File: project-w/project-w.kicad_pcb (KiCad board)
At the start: 2 copper layers, 17 parts, among them U1 NE555, U2 CD4017

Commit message: adding trace routes
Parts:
- removed BT1: Battery_Cell, Connectors_USB:USB_Micro-B_Wuerth-629105150521
- added J1: USB_A, Connectors_USB:USB_Micro-B_Molex-105017-0001, F.Cu at (184.2, 96.5)
- moved U2 50.9 mm to (180.3, 104.1)
- moved R3 48.7 mm to (176.5, 94.0), turned to 270 degrees
- moved C1 40.6 mm to (168.9, 96.5)
- moved U1 39.0 mm to (167.6, 114.3)
- moved R2 38.3 mm to (167.6, 109.2)
- moved R1 38.2 mm to (167.6, 104.1)
- moved D4 29.8 mm to (158.8, 111.8)
- moved D3 29.4 mm to (158.8, 104.1)
- moved D5 27.0 mm to (153.7, 118.1)
- moved D2 25.7 mm to (153.7, 97.8)
- moved D6 22.0 mm to (146.1, 120.7)
- moved D1 20.7 mm to (146.1, 94.0)
- moved D7 14.9 mm to (138.4, 118.1)
- moved D10 12.4 mm to (138.4, 97.8)
- moved D8 6.73 mm to (133.3, 111.8)
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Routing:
- net Net-(D1-Pad1): track 0.00 -> 100.8 mm
- net Net-(D2-Pad2): track 0.00 -> 67.4 mm, vias 0 -> 2
- net Net-(C1-Pad2): track 0.00 -> 64.7 mm, vias 0 -> 1
- net Net-(D10-Pad2): track 0.00 -> 64.0 mm, vias 0 -> 1
- net Net-(J1-Pad1): track 0.00 -> 56.6 mm, vias 0 -> 1
- net Net-(D5-Pad2): track 0.00 -> 50.5 mm, vias 0 -> 1
- net Net-(U1-Pad3): track 0.00 -> 50.5 mm
- net Net-(D1-Pad2): track 0.00 -> 50.1 mm
- net Net-(D8-Pad2): track 0.00 -> 47.6 mm
- net Net-(D9-Pad2): track 0.00 -> 46.6 mm
- net Net-(D7-Pad2): track 0.00 -> 45.2 mm, vias 0 -> 1
- net Net-(D6-Pad2): track 0.00 -> 39.9 mm
- net Net-(D3-Pad2): track 0.00 -> 38.8 mm
- net Net-(C1-Pad1): track 0.00 -> 35.2 mm
- net Net-(D4-Pad2): track 0.00 -> 28.8 mm
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
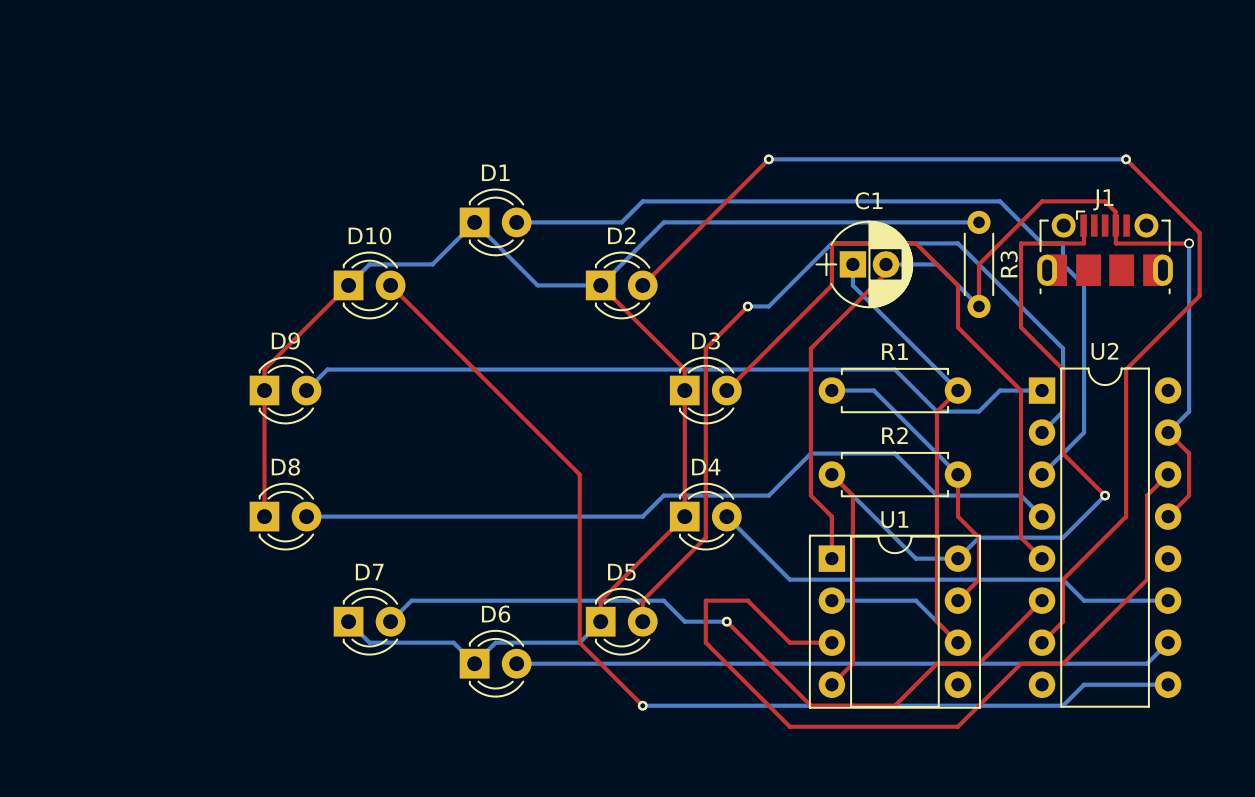
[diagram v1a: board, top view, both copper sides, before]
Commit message: adding more space for silk screening
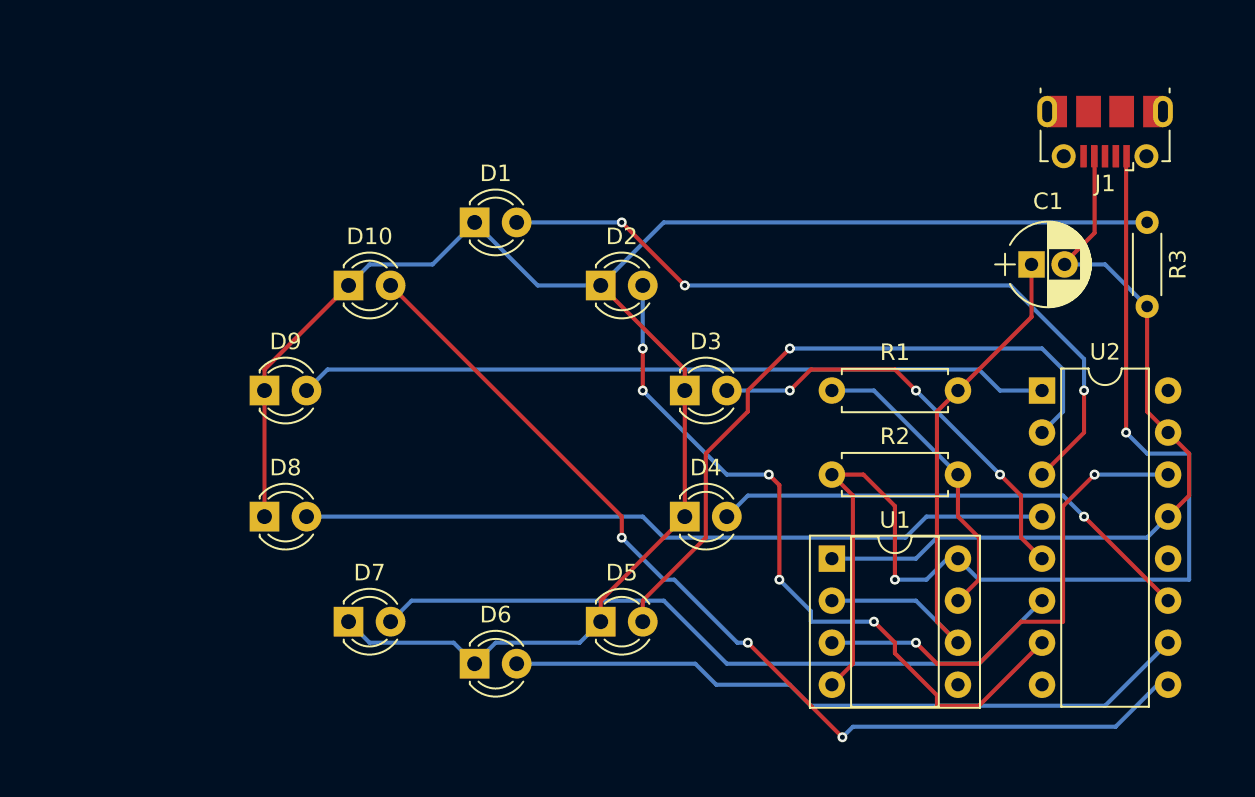
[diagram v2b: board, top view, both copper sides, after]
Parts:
- moved C1 10.8 mm to (179.7, 96.5)
- moved R3 10.2 mm to (186.7, 94.0)
- moved J1 8.89 mm to (184.2, 87.6), turned to 180 degrees
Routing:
- net Net-(D2-Pad2): track 67.4 -> 44.4 mm, vias 2 -> 5
- net Net-(U1-Pad3): track 50.5 -> 29.7 mm, vias 0 -> 2
- net Net-(C1-Pad2): track 64.7 -> 49.1 mm, vias 1 -> 0
- net Net-(J1-Pad1): track 56.6 -> 70.3 mm, vias 1 -> 2
- net Net-(D3-Pad2): track 38.8 -> 25.8 mm, vias 0 -> 3
- net Net-(D1-Pad1): track 100.8 -> 110.9 mm
- net Net-(D5-Pad2): track 50.5 -> 41.6 mm
- net Net-(D1-Pad2): track 50.1 -> 45.7 mm, vias 0 -> 3
- net Net-(D10-Pad2): track 64.0 -> 60.4 mm, vias 1 -> 3
- net Net-(D8-Pad2): track 47.6 -> 45.5 mm
- net Net-(D7-Pad2): track 45.2 -> 43.1 mm, vias 1 -> 0
- net Net-(D6-Pad2): track 39.9 -> 42.0 mm
- net Net-(D4-Pad2): track 28.8 -> 29.8 mm, vias 0 -> 1
- net Net-(D9-Pad2): track 46.6 -> 45.5 mm
- net Net-(C1-Pad1): track 35.2 -> 34.4 mm

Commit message: adding example text
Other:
- board text added: "Lorem Ipsum #0004"
- board text added: "blah blah __________________________ foo bar baz etc. etc. etc. etc."
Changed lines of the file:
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@@
     (area 131.974999 83.205 189.625 125.895002)
     (thickness 1.6)
-    (drawings 0)
+    (drawings 2)
     (tracks 170)
     (zones 0)
@@
     )
   )
+  (gr_text "blah blah __________________________\nfoo bar baz\netc. etc. etc. etc." (at 177.8 88.9) (layer B.SilkS)
+    (effects (font (size 1.5 1.5) (thickness 0.3)) (justify left mirror))
+  )
+  (gr_text "Lorem Ipsum #0004" (at 154.94 86.36) (layer F.SilkS)
+    (effects (font (size 2 2) (thickness 0.4)))
+  )
   (segment (start 175.26 104.14) (end 179.705 99.695) (width 0.25) (layer F.Cu) (net 1) (status 80000))

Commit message: trying to fix 3d models
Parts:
- J1: footprint Connectors_USB:USB_Micro-B_Molex-105017-0001 -> Connectors_USB:USB_Micro-B_Molex_47346-0001
- U1: footprint Housings_DIP:DIP-8_W7.62mm_Socket -> Housings_DIP:DIP-8_W7.62mm

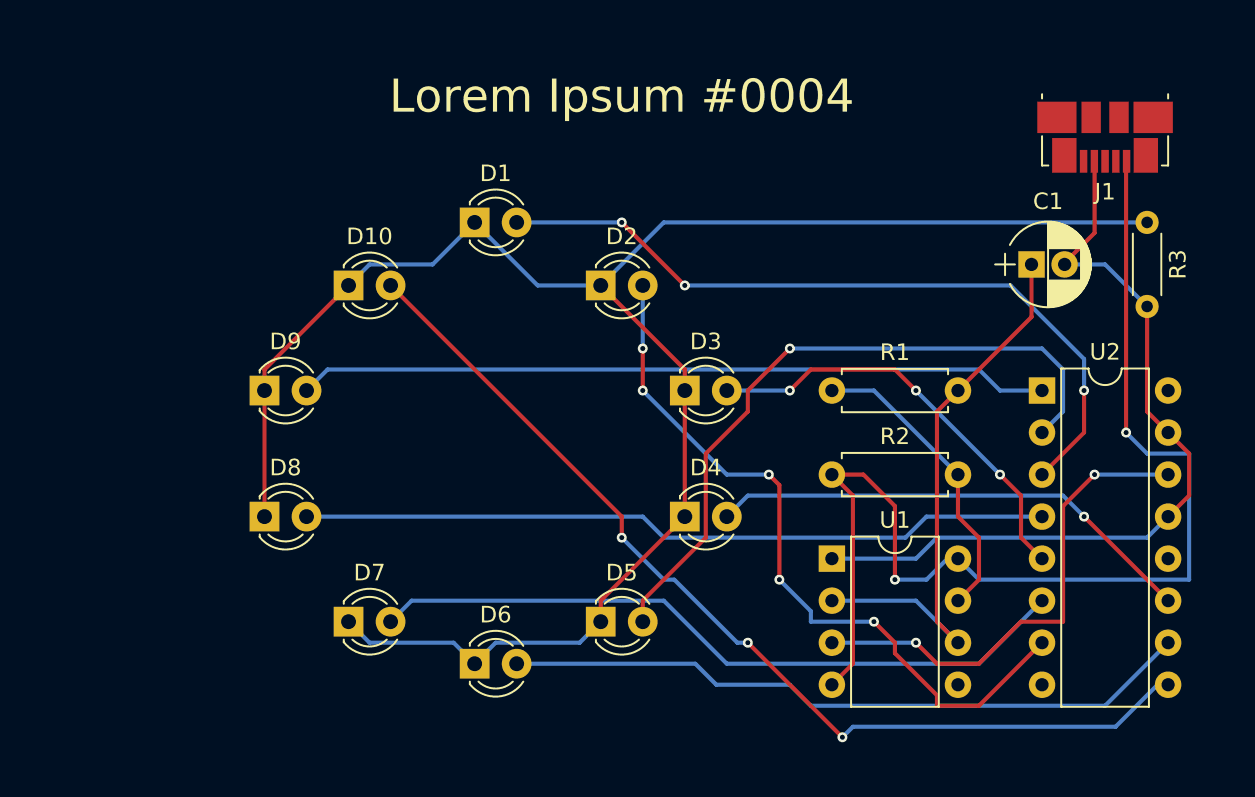
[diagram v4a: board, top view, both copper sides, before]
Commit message: updating schematic to fix VSS VDD issues
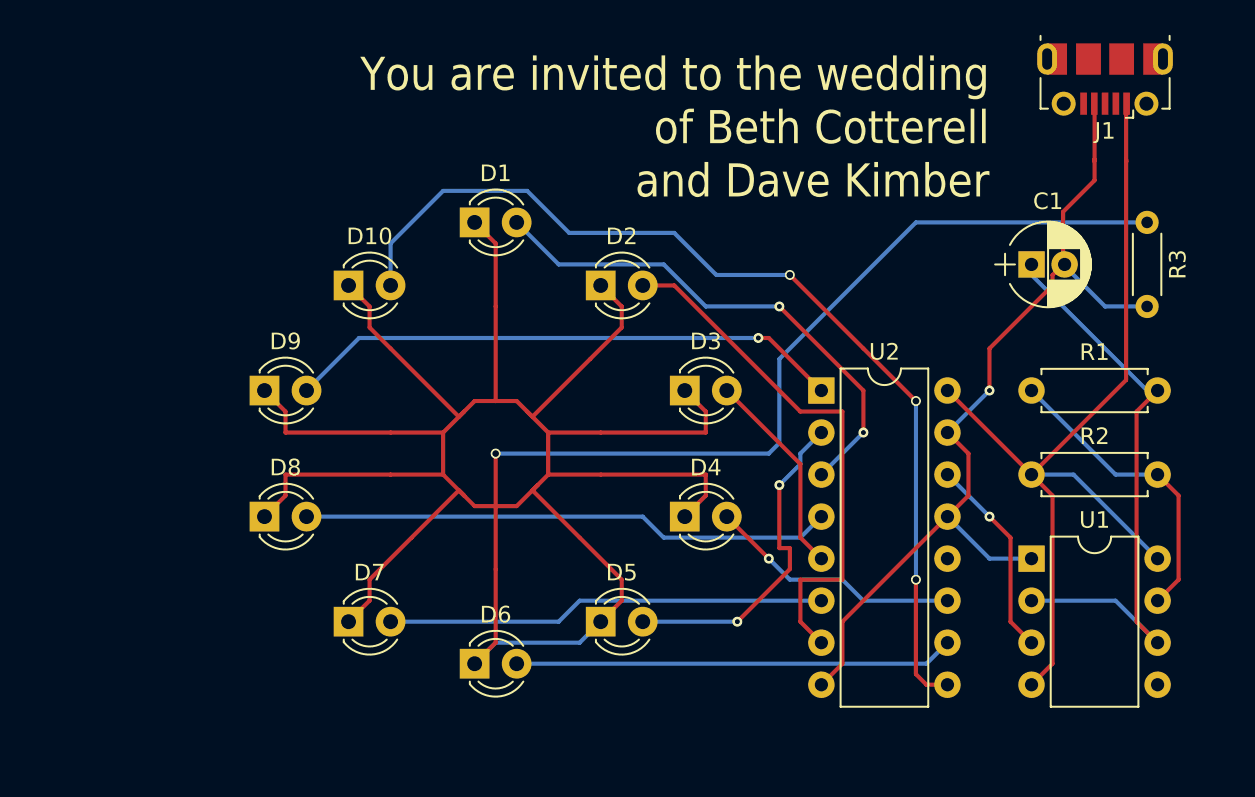
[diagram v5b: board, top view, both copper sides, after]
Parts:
- J1: footprint Connectors_USB:USB_Micro-B_Molex_47346-0001 -> Connectors_USB:USB_Micro-B_Molex-105017-0001
- R1: value 1K -> 47K
- moved U2 13.3 mm to (167.0, 104.1)
- moved R1 12.1 mm to (179.7, 104.1)
- moved R2 12.1 mm to (179.7, 109.2)
- moved U1 12.1 mm to (179.7, 114.3)
- moved J1 3.17 mm to (184.2, 84.5)
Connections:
- C1 pad 2: Net-(C1-Pad2) -> VSS
- J1 pad 1: Net-(J1-Pad1) -> VDD
- J1 pad 4: Net-(C1-Pad2) -> VSS
- R2 pad 1: Net-(J1-Pad1) -> VDD
- R3 pad 2: Net-(C1-Pad2) -> VSS
- U1 pad 1: Net-(C1-Pad2) -> VSS
- U1 pad 4: Net-(J1-Pad1) -> VDD
- U1 pad 8: Net-(J1-Pad1) -> VDD
- U2 pad 13: Net-(C1-Pad2) -> VSS
- U2 pad 15: Net-(C1-Pad2) -> VSS
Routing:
- net Net-(D1-Pad1): track 110.9 -> 197.2 mm, vias 0 -> 1
- net Net-(J1-Pad1): track 70.3 -> 0.00 mm, vias 2 -> 0
- net VSS: track 0.00 -> 55.7 mm, vias 0 -> 1
- net VDD: track 0.00 -> 55.6 mm
- net Net-(C1-Pad2): track 49.1 -> 0.00 mm
- net Net-(D5-Pad2): track 41.6 -> 20.1 mm, vias 1 -> 2
- net Net-(U1-Pad3): track 29.7 -> 12.3 mm, vias 2 -> 1
- net Net-(D7-Pad2): track 43.1 -> 26.6 mm
- net Net-(D6-Pad2): track 42.0 -> 26.6 mm
- net Net-(D1-Pad2): track 45.7 -> 31.3 mm, vias 3 -> 2
- net Net-(D4-Pad2): track 29.8 -> 15.4 mm
- net Net-(D8-Pad2): track 45.5 -> 32.2 mm
- net Net-(D3-Pad2): track 25.8 -> 12.5 mm, vias 3 -> 0
- net Net-(D2-Pad2): track 44.4 -> 32.3 mm, vias 5 -> 0
- net Net-(D9-Pad2): track 45.5 -> 33.7 mm, vias 0 -> 1
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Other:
- board text added: "15th September 2018 Manor Farm B&B BA3 4SG About 5ish"
- board text added: "You are invited to the wedding of Beth Cotterell and Dave Kimber"
- board text removed: "Lorem Ipsum #0004"
- board text removed: "blah blah __________________________ foo bar baz etc. etc. etc. etc."

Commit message: generated files for naked prototype
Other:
- board outline added: 62.9 x 44 mm
- board text added: "15th September 2018 blah blah blah About 5ish"
- board text removed: "15th September 2018 Manor Farm B&B BA3 4SG About 5ish"
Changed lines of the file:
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@@
     (area 131.974999 80.03 189.625 125.325)
     (thickness 1.6)
-    (drawings 2)
+    (drawings 9)
     (tracks 183)
     (zones 0)
@@
     )
   )
-  (gr_text "15th September 2018\n\nManor Farm B&B\nBA3 4SG\n\nAbout 5ish" (at 177.8 90.805) (layer B.SilkS)
+  (gr_text "15th September 2018\n\nblah blah blah\n\nAbout 5ish" (at 177.8 90.805) (layer B.SilkS)
     (effects (font (size 1.5 1.5) (thickness 0.3)) (justify left mirror))
   )
+  (gr_line (start 128.2065 82.6135) (end 128.4605 82.6135) (angle 90) (layer Edge.Cuts) (width 0.15))
+  (gr_line (start 128.2065 87.884) (end 128.2065 82.6135) (angle 90) (layer Edge.Cuts) (width 0.15))
+  (gr_line (start 187.0075 82.6135) (end 128.397 82.6135) (angle 90) (layer Edge.Cuts) (width 0.15))
+  (gr_line (start 128.2065 126.619) (end 128.2065 87.884) (angle 90) (layer Edge.Cuts) (width 0.15))
+  (gr_line (start 191.135 126.619) (end 128.2065 126.619) (angle 90) (layer Edge.Cuts) (width 0.15))
+  (gr_line (start 191.135 82.6135) (end 191.135 126.619) (angle 90) (layer Edge.Cuts) (width 0.15))
+  (gr_line (start 187.0075 82.6135) (end 191.135 82.6135) (angle 90) (layer Edge.Cuts) (width 0.15))
   (gr_text "You are invited to the wedding\nof Beth Cotterell\nand Dave Kimber" (at 177.165 88.265) (layer F.SilkS)
     (effects (font (size 2 1.8) (thickness 0.4)) (justify right))
@@
   (segment (start 178.435 113.03) (end 178.435 118.11) (width 0.25) (layer F.Cu) (net 15) (status 80000))
   (segment (start 178.435 118.11) (end 179.705 119.38) (width 0.25) (layer F.Cu) (net 15) (status 80000))
-  (segment (start 183.515 90.17) (end 183.515 86.82) (width 0.25) (layer F.Cu) (net 17) (status 800000))
-  (segment (start 183.515 86.82) (end 183.5 86.805) (width 0.25) (layer F.Cu) (net 17) (status C00000))
+  (segment (start 183.515 90.17) (end 183.515 86.82) (width 0.25) (layer F.Cu) (net 17))
+  (segment (start 183.515 86.82) (end 183.5 86.805) (width 0.25) (layer F.Cu) (net 17))
   (segment (start 174.625 111.76) (end 168.275 118.11) (width 0.25) (layer F.Cu) (net 17) (status 80000))
   (segment (start 168.275 118.11) (end 168.275 120.65) (width 0.25) (layer F.Cu) (net 17) (status 80000))
@@
   (segment (start 175.895 107.95) (end 175.895 110.49) (width 0.25) (layer F.Cu) (net 17) (status 80000))
   (segment (start 175.895 110.49) (end 174.625 111.76) (width 0.25) (layer F.Cu) (net 17) (status 80000))
-  (segment (start 185.42 90.17) (end 185.42 86.835) (width 0.25) (layer F.Cu) (net 18) (status 800000))
-  (segment (start 185.42 86.835) (end 185.45 86.805) (width 0.25) (layer F.Cu) (net 18) (status C00000))
+  (segment (start 185.42 90.17) (end 185.42 86.835) (width 0.25) (layer F.Cu) (net 18))
+  (segment (start 185.42 86.835) (end 185.45 86.805) (width 0.25) (layer F.Cu) (net 18))
   (segment (start 179.705 109.22) (end 185.42 103.505) (width 0.25) (layer F.Cu) (net 18) (status 80000))
   (segment (start 185.42 103.505) (end 185.42 90.17) (width 0.25) (layer F.Cu) (net 18) (status 80000))

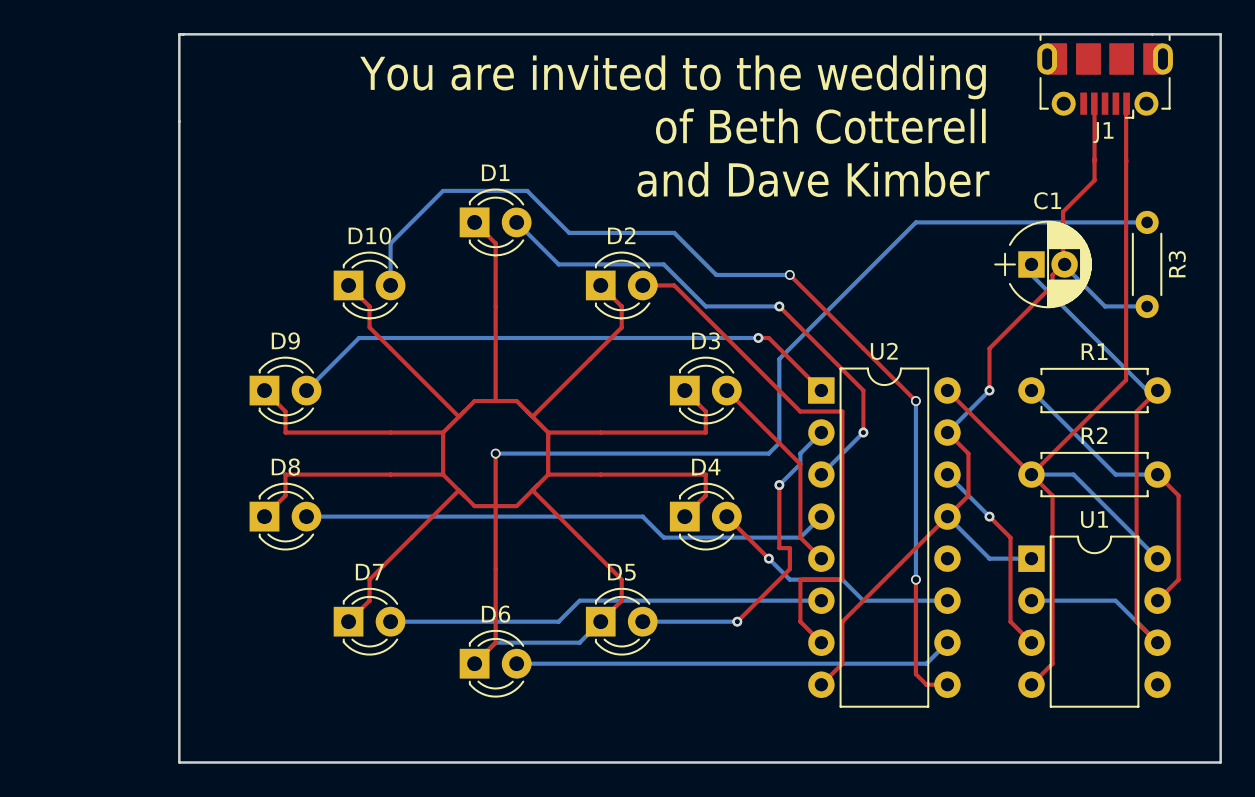
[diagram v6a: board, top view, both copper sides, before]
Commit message: updating schematic, fixing ordering issues, changin power connection
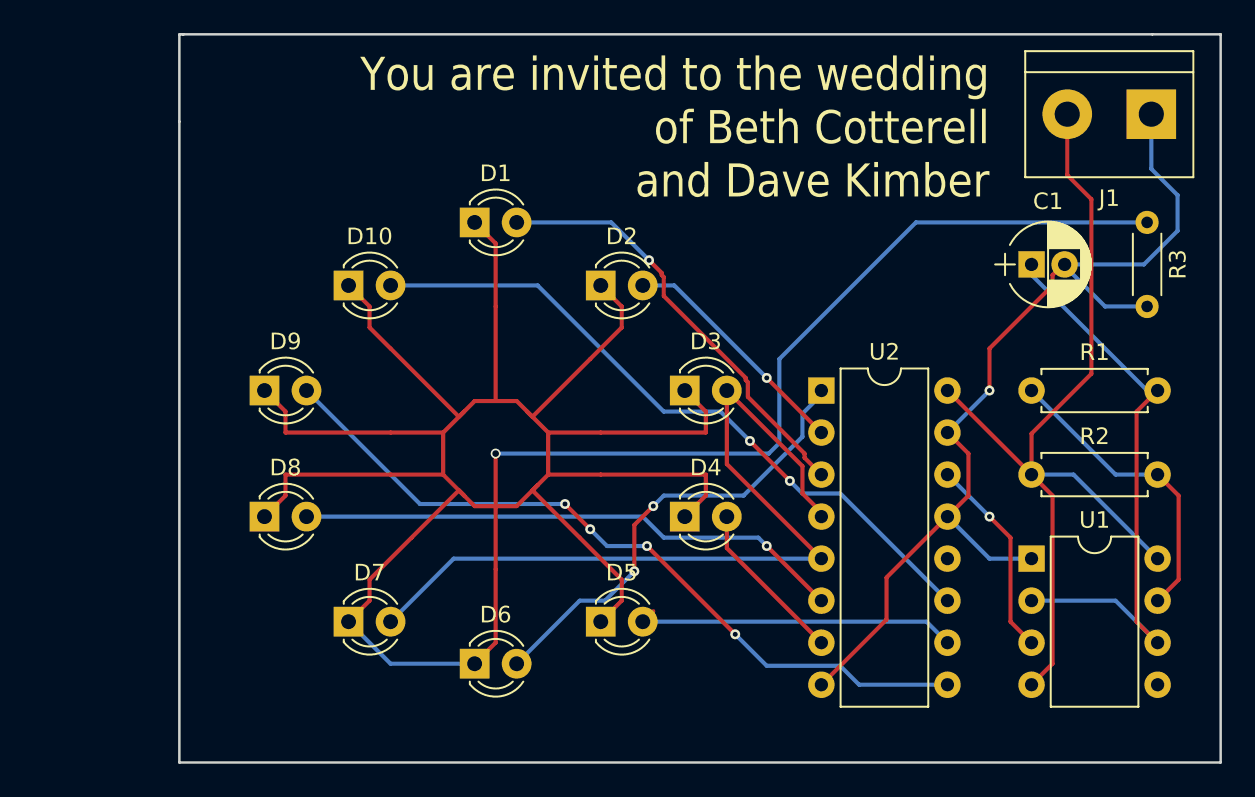
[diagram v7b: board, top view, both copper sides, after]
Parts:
- J1: value USB_A -> Screw_Terminal_01x02; footprint Connectors_USB:USB_Micro-B_Molex-105017-0001 -> Connectors_Terminal_Blocks:TerminalBlock_bornier-2_P5.08mm
- moved J1 4.09 mm to (186.9, 87.4)
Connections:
- J1 pad 1: VDD -> VSS
- J1 pad 2: Net-(J1-Pad2) -> VDD
- U2 pad 1: Net-(D9-Pad2) -> Net-(D6-Pad2)
- U2 pad 10: Net-(D6-Pad2) -> Net-(D5-Pad2)
- U2 pad 11: Net-(D4-Pad2) -> Net-(D10-Pad2)
- U2 pad 2: Net-(D5-Pad2) -> Net-(D2-Pad2)
- U2 pad 4: Net-(D8-Pad2) -> Net-(D3-Pad2)
- U2 pad 5: Net-(D3-Pad2) -> Net-(D7-Pad2)
- U2 pad 6: Net-(D7-Pad2) -> Net-(D8-Pad2)
- U2 pad 7: Net-(D2-Pad2) -> Net-(D4-Pad2)
- U2 pad 9: Net-(D10-Pad2) -> Net-(D9-Pad2)
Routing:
- net Net-(D10-Pad2): track 59.5 -> 41.5 mm, vias 3 -> 2
- net Net-(D2-Pad2): track 32.3 -> 14.5 mm, vias 0 -> 1
- net Net-(D9-Pad2): track 33.7 -> 46.8 mm, vias 1 -> 4
- net Net-(D7-Pad2): track 26.6 -> 35.7 mm
- net Net-(D4-Pad2): track 15.4 -> 10.2 mm, vias 1 -> 0
- net Net-(D1-Pad2): track 31.3 -> 26.2 mm, vias 2 -> 1
- net VSS: track 55.7 -> 60.4 mm
- net Net-(D3-Pad2): track 12.5 -> 14.4 mm
- net Net-(D6-Pad2): track 26.6 -> 28.0 mm, vias 0 -> 2
- net Net-(D8-Pad2): track 32.2 -> 33.2 mm, vias 0 -> 1
- net VDD: track 55.6 -> 54.5 mm
- net Net-(D5-Pad2): track 20.1 -> 19.8 mm, vias 2 -> 0

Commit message: fixes for prototype version 3
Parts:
- R3: value 470R -> 1K
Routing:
- net Net-(D7-Pad2): track 35.7 -> 27.6 mm
- net Net-(D3-Pad2): track 14.4 -> 9.99 mm
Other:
- board text added: "15/09/18"
- board text added: "Please join us for the ceremony followed by an evening river cruise with food, drinks and dancing"
- board text added: "RSVP: lordkimber@gmail.com by 31/08/18"
- board text removed: "15th September 2018 blah blah blah About 5ish"
